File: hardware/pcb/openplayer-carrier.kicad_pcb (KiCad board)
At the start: 2 copper layers, 60 x 45 mm, 15 parts, among them J1 Pi_40pin_IDC, J2 PWR_IN, J3 KEY, J4 BUTTONS, J5 DISPLAY, J6 SWITCH

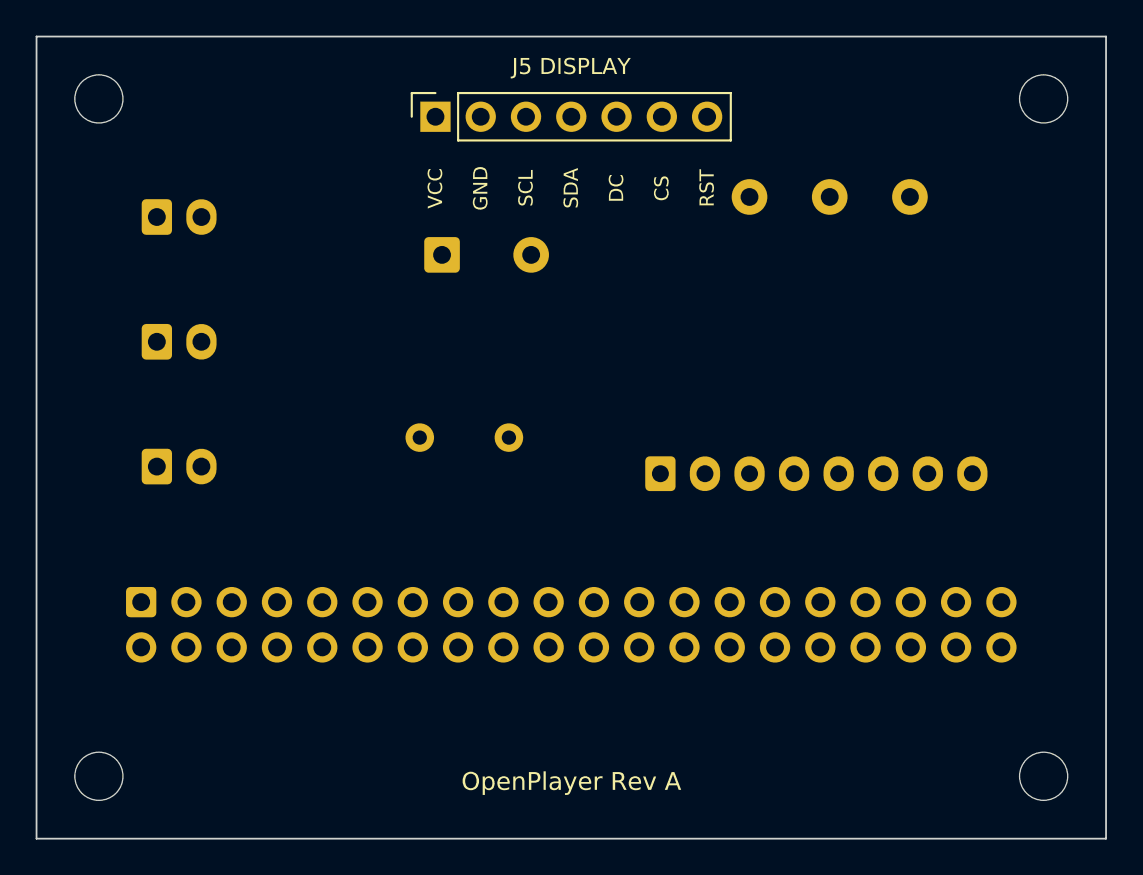
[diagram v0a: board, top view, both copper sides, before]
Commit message: Add routing functionality to PCB build script
- Implemented a grid-based router using Dijkstra's algorithm for routing tracks on F.Cu and B.Cu layers.
- Introduced new constants for track widths, clearance, and via dimensions.
- Added a Router class to manage routing logic, including pathfinding and obstacle handling.
- Enhanced the build process to include routing of specified nets in a defined order.
- Integrated ground stitching vias to ensure connectivity between ground pours on both layers.
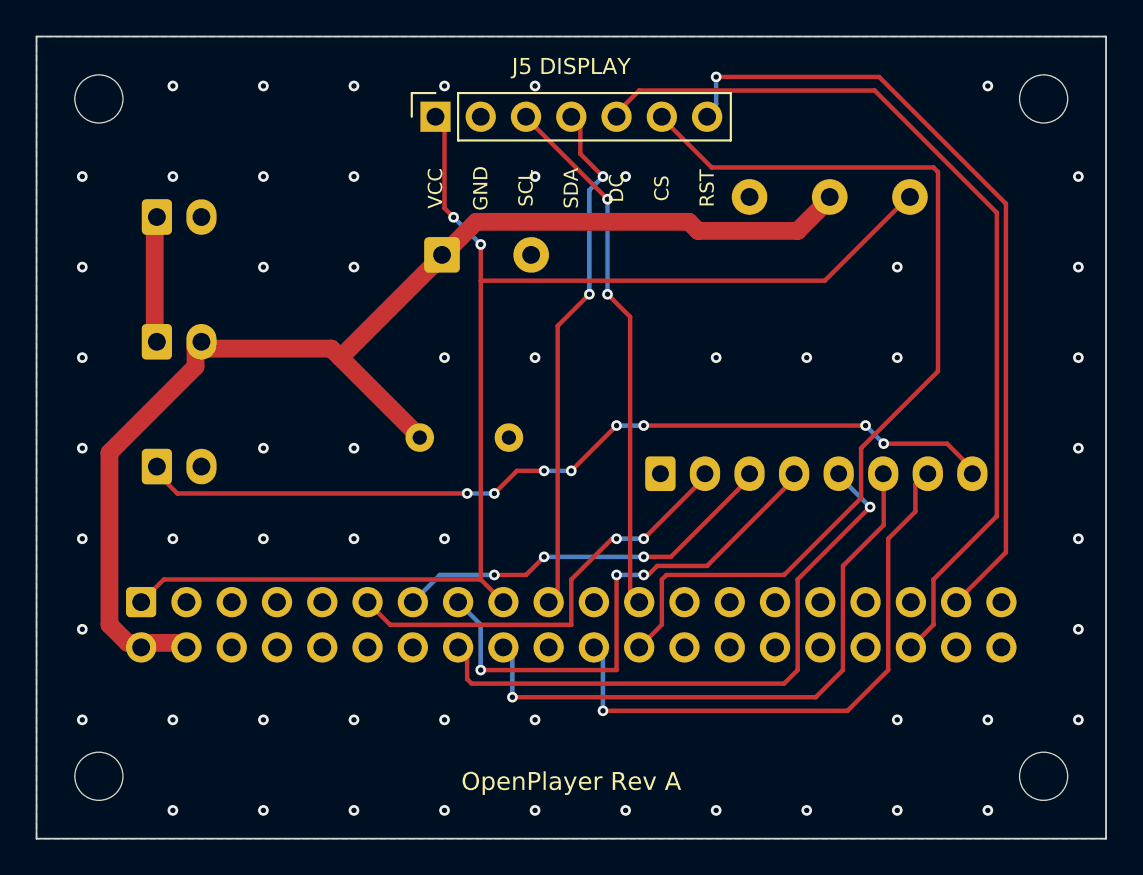
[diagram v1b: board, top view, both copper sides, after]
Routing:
- net /3V3: track 0.00 -> 74.4 mm, vias 0 -> 2
- net /5V_SYS: track 0.00 -> 69.3 mm
- net /LCD_CS: track 0.00 -> 54.3 mm
- net /LCD_DC: track 0.00 -> 51.2 mm
- net /PWR_KEY: track 0.00 -> 49.3 mm, vias 0 -> 8
- net /LCD_RST: track 0.00 -> 45.1 mm, vias 0 -> 1
- net /BTN_VOLUP: track 0.00 -> 34.4 mm, vias 0 -> 1
- net /BTN_VOLDN: track 0.00 -> 34.1 mm, vias 0 -> 1
- net /BTN_MENU: track 0.00 -> 32.7 mm, vias 0 -> 1
- net /SPI_SCLK: track 0.00 -> 29.8 mm, vias 0 -> 2
- net /BTN_NEXT: track 0.00 -> 29.7 mm, vias 0 -> 3
- net /SPI_MOSI: track 0.00 -> 29.2 mm, vias 0 -> 2
- net /BTN_PLAY: track 0.00 -> 24.5 mm, vias 0 -> 2
- net /BTN_PREV: track 0.00 -> 22.0 mm, vias 0 -> 3
- net /5V_IN: track 0.00 -> 7.04 mm
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- added copper zone on B.Cu, net /GND
- added copper zone on F.Cu, net /GND
